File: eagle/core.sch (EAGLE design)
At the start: 26 parts, among them T1 BC846, T2 BC846, T3 BC846, T4 BC846

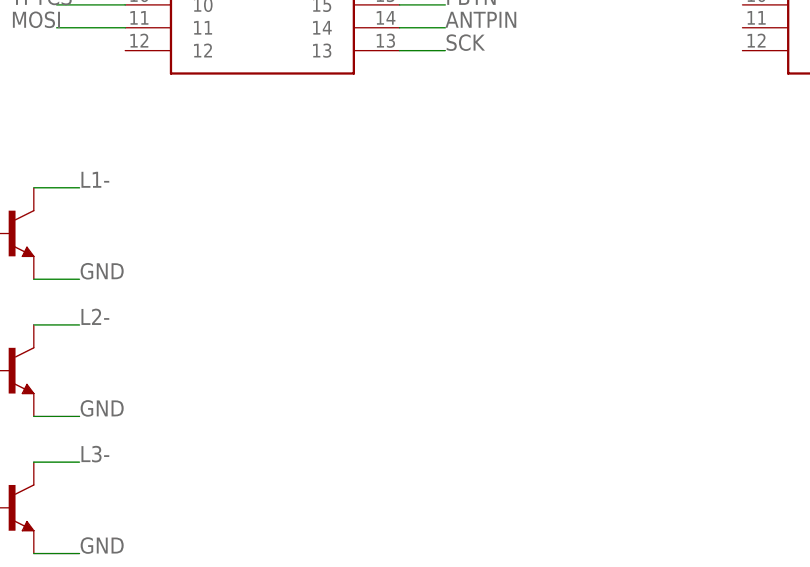
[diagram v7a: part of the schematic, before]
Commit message: Added optional I2C pullups and started renderer.
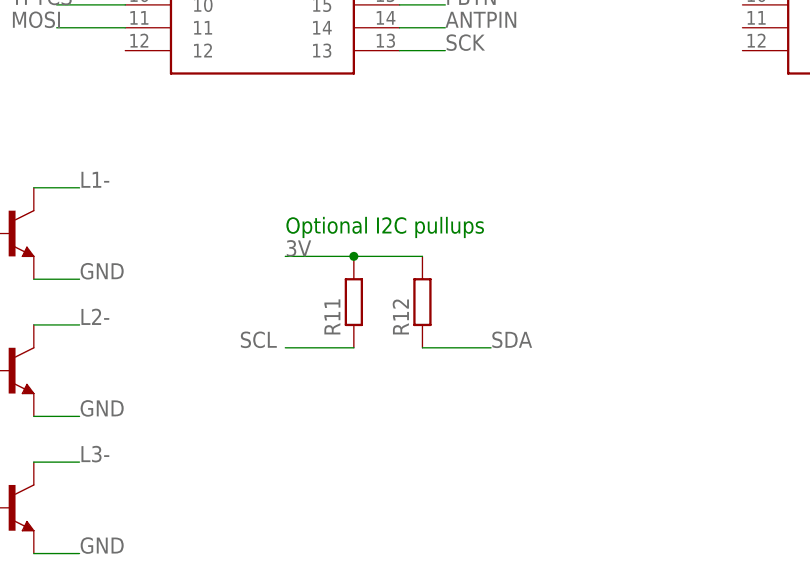
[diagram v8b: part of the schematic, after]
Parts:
- added R11, R12: (no value), resistor:R-EU_R0805
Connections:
- net 3V: now also R11.2, R12.2
- net SCL: now also R11.1
- net SDA: now also R12.1
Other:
- note added: "Optional I2C pullups"
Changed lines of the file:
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@@
 <part name="ENCR" library="testpad" library_urn="urn:adsk.eagle:library:385" deviceset="TP" device="TP14R" package3d_urn="urn:adsk.eagle:package:27966/1"/>
 <part name="ENCL" library="testpad" library_urn="urn:adsk.eagle:library:385" deviceset="TP" device="TP14R" package3d_urn="urn:adsk.eagle:package:27966/1"/>
+<part name="R11" library="resistor" library_urn="urn:adsk.eagle:library:348" deviceset="R-EU_" device="R0805" package3d_urn="urn:adsk.eagle:package:23553/2"/>
+<part name="R12" library="resistor" library_urn="urn:adsk.eagle:library:348" deviceset="R-EU_" device="R0805" package3d_urn="urn:adsk.eagle:package:23553/2"/>
 </parts>
 <sheets>
@@
 <text x="-48.26" y="83.82" size="1.778" layer="91">Teensy 4</text>
 <text x="20.32" y="83.82" size="1.778" layer="91">Teensy 3.2</text>
+<text x="-40.64" y="25.4" size="1.778" layer="91">Optional I2C pullups</text>
 </plain>
 <instances>
@@
 <attribute name="NAME" x="-138.43" y="36.83" size="1.778" layer="95" rot="R180"/>
 <attribute name="TP_SIGNAL_NAME" x="-140.97" y="39.37" size="1.778" layer="97" rot="R180"/>
+</instance>
+<instance part="R11" gate="G$1" x="-33.02" y="17.78" smashed="yes" rot="R90">
+<attribute name="NAME" x="-34.5186" y="13.97" size="1.778" layer="95" rot="R90"/>
+<attribute name="VALUE" x="-29.718" y="13.97" size="1.778" layer="96" rot="R90"/>
+</instance>
+<instance part="R12" gate="G$1" x="-25.4" y="17.78" smashed="yes" rot="R90">
+<attribute name="NAME" x="-26.8986" y="13.97" size="1.778" layer="95" rot="R90"/>
+<attribute name="VALUE" x="-22.098" y="13.97" size="1.778" layer="96" rot="R90"/>
 </instance>
 </instances>
@@
 <label x="-149.86" y="12.7" size="1.778" layer="95"/>
 </segment>
+<segment>
+<pinref part="R11" gate="G$1" pin="2"/>
+<wire x1="-33.02" y1="22.86" x2="-40.64" y2="22.86" width="0.1524" layer="91"/>
+<pinref part="R12" gate="G$1" pin="2"/>
+<wire x1="-33.02" y1="22.86" x2="-25.4" y2="22.86" width="0.1524" layer="91"/>
+<junction x="-33.02" y="22.86"/>
+<label x="-40.64" y="22.86" size="1.778" layer="95"/>
+</segment>
 </net>
 <net name="ENCL" class="0">
@@
 <label x="-175.26" y="-12.7" size="1.778" layer="95"/>
 </segment>
+<segment>
+<pinref part="R12" gate="G$1" pin="1"/>
+<wire x1="-25.4" y1="12.7" x2="-17.78" y2="12.7" width="0.1524" layer="91"/>
+<label x="-17.78" y="12.7" size="1.778" layer="95"/>
+</segment>
 </net>
 <net name="SCL" class="0">
@@
 <label x="-175.26" y="-15.24" size="1.778" layer="95"/>
 </segment>
-</net>
+<segment>
+<pinref part="R11" gate="G$1" pin="1"/>
+<wire x1="-33.02" y1="12.7" x2="-40.64" y2="12.7" width="0.1524" layer="91"/>
+<label x="-45.72" y="12.7" size="1.778" layer="95"/>
+</segment>
+</net>
